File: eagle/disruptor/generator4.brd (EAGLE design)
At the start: 126.5 x 120.7 mm, 35 parts, among them IC1 NE555, IC2 74ALS04N, IC3 IR2110, IC4 7805TV, J1 PIN2F061.100, J2 PIN2F061.100, J3 PIN2F061.100, J4 PIN2F061.100, J5 PIN2F061.100, J6 PIN2F061.100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

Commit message: gen4b
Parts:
- added C14, C15: 1u, rcl:E5-8,5
- R6, R7: value 1M -> 22k
- moved J1 2.34 mm to (69.1, 19.1)
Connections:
- new net N$8: C14.-, C15.+, J2.A1, J2.A2
- net GND: now also C15.-; no longer J2.A1, J2.A2
- net N$6: now also C14.+
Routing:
- net TRANS: track 24.1 -> 207.0 mm
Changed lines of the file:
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@@
 <element name="R4" library="rcl" package="0207/10" value="100" x="45.72" y="29.21"/>
 <element name="R5" library="rcl" package="0207/10" value="100" x="50.8" y="10.16" rot="R90"/>
-<element name="J1" library="con-faston" package="F061.100" value="PIN2F061.100" x="68.58" y="21.336" rot="R180">
-<attribute name="OC_NEWARK" value="unknown" x="68.58" y="21.336" size="1.778" layer="27" rot="R180" display="off"/>
-<attribute name="MPN" value="" x="68.58" y="21.336" size="1.778" layer="27" rot="R180" display="off"/>
-<attribute name="MF" value="" x="68.58" y="21.336" size="1.778" layer="27" rot="R180" display="off"/>
-<attribute name="OC_FARNELL" value="unknown" x="68.58" y="21.336" size="1.778" layer="27" rot="R180" display="off"/>
+<element name="J1" library="con-faston" package="F061.100" value="PIN2F061.100" x="69.088" y="19.05" rot="R180">
+<attribute name="OC_NEWARK" value="unknown" x="69.088" y="19.05" size="1.778" layer="27" rot="R180" display="off"/>
+<attribute name="MPN" value="" x="69.088" y="19.05" size="1.778" layer="27" rot="R180" display="off"/>
+<attribute name="MF" value="" x="69.088" y="19.05" size="1.778" layer="27" rot="R180" display="off"/>
+<attribute name="OC_FARNELL" value="unknown" x="69.088" y="19.05" size="1.778" layer="27" rot="R180" display="off"/>
 </element>
 <element name="J2" library="con-faston" package="F061.100" value="PIN2F061.100" x="68.58" y="5.588" rot="R180">
@@
 <attribute name="OC_FARNELL" value="unknown" x="-40.386" y="86.868" size="1.778" layer="27" display="off"/>
 </element>
-<element name="R6" library="rcl" package="0207/10" value="1M" x="36.576" y="24.13" rot="R270"/>
-<element name="R7" library="rcl" package="0207/10" value="1M" x="18.288" y="5.08" rot="R180"/>
+<element name="R6" library="rcl" package="0207/10" value="22k" x="36.576" y="24.13" rot="R270"/>
+<element name="R7" library="rcl" package="0207/10" value="22k" x="18.288" y="5.08" rot="R180"/>
 <element name="C3" library="rcl" package="C075-052X106" value="10n" x="29.972" y="64.77" rot="R180"/>
 <element name="C6" library="rcl" package="C075-052X106" value="10n" x="53.848" y="42.926" rot="R180"/>
@@
 <element name="B2" library="rectifier" package="GBU4" value="RECTIFIER-GBU4" x="-22.86" y="78.994" rot="R270"/>
 <element name="C13" library="resistor" package="E7,5-18" value="" x="-2.286" y="106.934" rot="R90"/>
+<element name="C14" library="rcl" package="E5-8,5" value="1u" x="92.71" y="7.874" rot="R270"/>
+<element name="C15" library="rcl" package="E5-8,5" value="1u" x="94.996" y="23.622" rot="R90"/>
 </elements>
 <signals>
@@
 <contactref element="C2" pad="-"/>
 <contactref element="C4" pad="-"/>
-<contactref element="Q2" pad="S"/>
 <contactref element="R7" pad="2"/>
 <contactref element="C3" pad="1"/>
@@
 <wire x1="60.198" y1="58.674" x2="55.118" y2="53.594" width="1.6764" layer="16"/>
 <wire x1="55.118" y1="53.594" x2="55.118" y2="50.038" width="1.6764" layer="16"/>
-<contactref element="J2" pad="A1"/>
-<contactref element="J2" pad="A2"/>
+<contactref element="C15" pad="-"/>
+<contactref element="Q2" pad="S"/>
+<wire x1="60.198" y1="63.5" x2="60.198" y2="71.12" width="0" layer="19" extent="1-1"/>
+<wire x1="94.996" y1="26.162" x2="57.658" y2="42.926" width="0" layer="19" extent="1-1"/>
 </signal>
 <signal name="VCC">
@@
 <wire x1="22.098" y1="19.05" x2="36.576" y2="19.05" width="1.6764" layer="1"/>
 <wire x1="52.578" y1="80.01" x2="52.578" y2="77.47" width="2.54" layer="1"/>
-<wire x1="52.578" y1="77.47" x2="52.578" y2="70.358" width="1.6764" layer="1"/>
+<wire x1="36.576" y1="19.05" x2="31.75" y2="19.05" width="1.6764" layer="1"/>
+<wire x1="31.75" y1="19.05" x2="31.75" y2="7.62" width="1.6764" layer="1"/>
+<wire x1="31.75" y1="7.62" x2="37.084" y2="7.62" width="1.6764" layer="1"/>
+<wire x1="52.578" y1="70.358" x2="52.578" y2="77.47" width="1.6764" layer="1"/>
+<wire x1="71.12" y1="74.93" x2="71.12" y2="20.828" width="2.54" layer="1"/>
+<wire x1="36.576" y1="19.05" x2="56.134" y2="19.05" width="2.54" layer="1"/>
+<wire x1="56.134" y1="19.05" x2="66.588" y2="19.05" width="2.54" layer="1"/>
+<wire x1="71.12" y1="74.93" x2="53.086" y2="74.93" width="2.54" layer="1"/>
+<wire x1="66.588" y1="19.05" x2="74.168" y2="19.05" width="1.6764" layer="1"/>
+<wire x1="74.168" y1="19.05" x2="74.168" y2="21.082" width="1.6764" layer="1"/>
+<wire x1="74.168" y1="21.082" x2="63.754" y2="21.082" width="1.6764" layer="1"/>
+<wire x1="63.754" y1="21.082" x2="63.5" y2="20.828" width="1.6764" layer="1"/>
+<wire x1="63.5" y1="20.828" x2="63.5" y2="17.018" width="1.6764" layer="1"/>
+<wire x1="63.5" y1="17.018" x2="74.168" y2="17.018" width="1.6764" layer="1"/>
+<wire x1="74.168" y1="17.018" x2="74.168" y2="19.304" width="1.6764" layer="1"/>
+<wire x1="74.168" y1="19.304" x2="73.914" y2="19.558" width="1.6764" layer="1"/>
+<wire x1="73.914" y1="19.558" x2="64.77" y2="19.558" width="1.6764" layer="1"/>
+<wire x1="64.77" y1="19.558" x2="64.262" y2="20.066" width="1.6764" layer="1"/>
+<wire x1="64.262" y1="20.066" x2="64.262" y2="18.034" width="1.6764" layer="1"/>
+<wire x1="64.262" y1="18.034" x2="64.516" y2="17.78" width="1.6764" layer="1"/>
+<wire x1="64.516" y1="17.78" x2="73.914" y2="17.78" width="1.6764" layer="1"/>
 <wire x1="52.578" y1="70.358" x2="52.578" y2="71.12" width="0" layer="19" extent="1-1"/>
-<wire x1="66.08" y1="21.336" x2="52.578" y2="70.358" width="0" layer="19" extent="1-1"/>
-<wire x1="71.08" y1="21.336" x2="66.08" y2="21.336" width="0" layer="19" extent="1-1"/>
-<wire x1="36.576" y1="19.05" x2="66.08" y2="21.336" width="0" layer="19" extent="1-1"/>
-<wire x1="36.068" y1="7.62" x2="36.576" y2="19.05" width="0" layer="19" extent="1-1"/>
+<wire x1="53.086" y1="74.93" x2="52.578" y2="77.47" width="0" layer="19" extent="1-1"/>
+<wire x1="71.588" y1="19.05" x2="71.12" y2="20.828" width="0" layer="19" extent="1-1"/>
+<wire x1="73.914" y1="19.558" x2="71.588" y2="19.05" width="0" layer="19" extent="1-1"/>
+<wire x1="36.068" y1="7.62" x2="37.084" y2="7.62" width="0" layer="19" extent="1-1"/>
 </signal>
 <signal name="N$3">
@@
 <wire x1="10.414" y1="18.542" x2="13.462" y2="21.59" width="2.54" layer="1"/>
 <wire x1="13.462" y1="21.59" x2="22.606" y2="21.59" width="1.6764" layer="1"/>
-<wire x1="22.606" y1="21.59" x2="22.098" y2="21.59" width="0" layer="19" extent="1-1"/>
+<contactref element="C14" pad="+"/>
+<wire x1="22.606" y1="21.59" x2="92.71" y2="10.414" width="0" layer="19" extent="1-1"/>
+<wire x1="22.098" y1="21.59" x2="22.606" y2="21.59" width="0" layer="19" extent="1-1"/>
+</signal>
+<signal name="N$8">
+<contactref element="J2" pad="A1"/>
+<contactref element="J2" pad="A2"/>
+<contactref element="C15" pad="+"/>
+<contactref element="C14" pad="-"/>
+<wire x1="92.71" y1="5.334" x2="94.996" y2="21.082" width="0" layer="19" extent="1-1"/>
+<wire x1="71.08" y1="5.588" x2="92.71" y2="5.334" width="0" layer="19" extent="1-1"/>
+<wire x1="66.08" y1="5.588" x2="71.08" y2="5.588" width="0" layer="19" extent="1-1"/>
 </signal>
 </signals>

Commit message: generator 4 is the correct way.
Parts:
- C14, C15: value 1u -> 50u
- C7: value 1u -> min 12 nF
- R4, R5: value 100 -> 10
- moved C15 39.9 mm to (55.9, 16.0), turned to 180 degrees
- moved C14 36.9 mm to (55.9, 5.84), turned to 0 degrees
- moved J1 5.59 mm to (68.8, 24.6)
- moved R5 4.58 mm to (46.2, 9.91)
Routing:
- net TRANS: track 207.0 -> 27.7 mm
- net LO: track 69.6 -> 1.52 mm
- net N$11: track 29.5 -> 2.03 mm
- net N$12: track 20.6 -> 0.00 mm
- net HO: track 72.2 -> 54.9 mm
- net N$6: track 91.1 -> 77.6 mm
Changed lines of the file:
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@@
 <element name="D1" library="diode" package="D-7.5" value="UF4004" x="57.658" y="88.9"/>
 <element name="C8" library="rcl" package="E5-8,5" value="1u" x="61.468" y="82.296" rot="R270"/>
-<element name="C7" library="rcl" package="E5-8,5" value="1u" x="50.038" y="80.01"/>
+<element name="C7" library="rcl" package="E5-8,5" value="min 12 nF" x="50.038" y="80.01"/>
 <element name="IC1" library="st-microelectronics" package="DIL-08" value="NE555" x="17.018" y="59.69">
 <attribute name="OC_NEWARK" value="89K1486" x="76.708" y="-11.43" size="1.778" layer="27" display="off"/>
@@
 <element name="C4" library="rcl" package="E5-8,5" value="1u" x="67.818" y="112.014" rot="R270"/>
 <element name="C5" library="rcl" package="E5-8,5" value="1u" x="67.818" y="99.06" rot="R90"/>
-<element name="R4" library="rcl" package="0207/10" value="100" x="45.72" y="29.21"/>
-<element name="R5" library="rcl" package="0207/10" value="100" x="50.8" y="10.16" rot="R90"/>
-<element name="J1" library="con-faston" package="F061.100" value="PIN2F061.100" x="69.088" y="19.05" rot="R180">
-<attribute name="OC_NEWARK" value="unknown" x="69.088" y="19.05" size="1.778" layer="27" rot="R180" display="off"/>
-<attribute name="MPN" value="" x="69.088" y="19.05" size="1.778" layer="27" rot="R180" display="off"/>
-<attribute name="MF" value="" x="69.088" y="19.05" size="1.778" layer="27" rot="R180" display="off"/>
-<attribute name="OC_FARNELL" value="unknown" x="69.088" y="19.05" size="1.778" layer="27" rot="R180" display="off"/>
+<element name="R4" library="rcl" package="0207/10" value="10" x="45.72" y="29.21"/>
+<element name="R5" library="rcl" package="0207/10" value="10" x="46.228" y="9.906" rot="R90"/>
+<element name="J1" library="con-faston" package="F061.100" value="PIN2F061.100" x="68.834" y="24.638" rot="R180">
+<attribute name="OC_NEWARK" value="unknown" x="68.834" y="24.638" size="1.778" layer="27" rot="R180" display="off"/>
+<attribute name="MPN" value="" x="68.834" y="24.638" size="1.778" layer="27" rot="R180" display="off"/>
+<attribute name="MF" value="" x="68.834" y="24.638" size="1.778" layer="27" rot="R180" display="off"/>
+<attribute name="OC_FARNELL" value="unknown" x="68.834" y="24.638" size="1.778" layer="27" rot="R180" display="off"/>
 </element>
 <element name="J2" library="con-faston" package="F061.100" value="PIN2F061.100" x="68.58" y="5.588" rot="R180">
@@
 <element name="B2" library="rectifier" package="GBU4" value="RECTIFIER-GBU4" x="-22.86" y="78.994" rot="R270"/>
 <element name="C13" library="resistor" package="E7,5-18" value="" x="-2.286" y="106.934" rot="R90"/>
-<element name="C14" library="rcl" package="E5-8,5" value="1u" x="92.71" y="7.874" rot="R270"/>
-<element name="C15" library="rcl" package="E5-8,5" value="1u" x="94.996" y="23.622" rot="R90"/>
+<element name="C14" library="rcl" package="E5-8,5" value="50u" x="55.88" y="5.842"/>
+<element name="C15" library="rcl" package="E5-8,5" value="50u" x="55.88" y="16.002" rot="R180"/>
 </elements>
 <signals>
@@
 <contactref element="Q2" pad="S"/>
 <wire x1="60.198" y1="63.5" x2="60.198" y2="71.12" width="0" layer="19" extent="1-1"/>
-<wire x1="94.996" y1="26.162" x2="57.658" y2="42.926" width="0" layer="19" extent="1-1"/>
 </signal>
 <signal name="VCC">
@@
 <contactref element="IC3" pad="1"/>
 <contactref element="R5" pad="2"/>
-<wire x1="62.738" y1="33.02" x2="50.8" y2="21.59" width="1.6764" layer="16"/>
-<wire x1="50.8" y1="21.59" x2="50.8" y2="15.24" width="1.6764" layer="16"/>
 <wire x1="62.738" y1="71.12" x2="62.738" y2="72.644" width="1.6764" layer="16"/>
-<wire x1="62.738" y1="71.12" x2="62.738" y2="67.31" width="1.6764" layer="16"/>
-<wire x1="62.738" y1="67.31" x2="66.294" y2="67.31" width="1.6764" layer="16"/>
-<wire x1="66.294" y1="67.31" x2="66.294" y2="33.02" width="1.6764" layer="16"/>
-<wire x1="66.294" y1="33.02" x2="62.738" y2="33.02" width="1.6764" layer="16"/>
+<wire x1="46.228" y1="14.986" x2="62.738" y2="71.12" width="0" layer="19" extent="1-1"/>
 </signal>
 <signal name="HO">
@@
 <wire x1="47.498" y1="67.31" x2="65.532" y2="67.31" width="1.6764" layer="1"/>
 <wire x1="65.532" y1="67.31" x2="65.532" y2="35.56" width="2.54" layer="1"/>
-<wire x1="65.532" y1="35.56" x2="57.15" y2="35.56" width="2.54" layer="1"/>
-<wire x1="57.15" y1="35.56" x2="50.8" y2="29.21" width="2.54" layer="1"/>
+<wire x1="50.8" y1="29.21" x2="65.532" y2="35.56" width="0" layer="19" extent="1-1"/>
 </signal>
 <signal name="N$17">
@@
 <contactref element="Q2" pad="G"/>
 <contactref element="R7" pad="1"/>
-<wire x1="23.368" y1="5.08" x2="36.068" y2="5.08" width="1.6764" layer="1"/>
 <wire x1="36.068" y1="5.08" x2="38.1" y2="5.08" width="1.6764" layer="1"/>
-<wire x1="36.068" y1="5.08" x2="50.8" y2="5.08" width="1.6764" layer="1"/>
+<wire x1="38.1" y1="5.08" x2="46.228" y2="4.826" width="0" layer="19" extent="1-1"/>
+<wire x1="23.368" y1="5.08" x2="36.068" y2="5.08" width="0" layer="19" extent="1-1"/>
 </signal>
 <signal name="N$12">
@@
 <contactref element="R4" pad="1"/>
 <contactref element="R6" pad="1"/>
-<wire x1="22.098" y1="24.13" x2="31.496" y2="24.13" width="1.6764" layer="1"/>
-<wire x1="31.496" y1="24.13" x2="36.576" y2="29.21" width="1.6764" layer="1"/>
-<wire x1="36.576" y1="29.21" x2="40.64" y2="29.21" width="1.6764" layer="1"/>
+<wire x1="36.576" y1="29.21" x2="40.64" y2="29.21" width="0" layer="19" extent="1-1"/>
+<wire x1="22.098" y1="24.13" x2="36.576" y2="29.21" width="0" layer="19" extent="1-1"/>
 </signal>
 <signal name="TRANS">
@@
 <contactref element="J1" pad="A1"/>
 <contactref element="J1" pad="A2"/>
-<wire x1="22.098" y1="19.05" x2="36.576" y2="19.05" width="1.6764" layer="1"/>
 <wire x1="52.578" y1="80.01" x2="52.578" y2="77.47" width="2.54" layer="1"/>
-<wire x1="36.576" y1="19.05" x2="31.75" y2="19.05" width="1.6764" layer="1"/>
-<wire x1="31.75" y1="19.05" x2="31.75" y2="7.62" width="1.6764" layer="1"/>
-<wire x1="31.75" y1="7.62" x2="37.084" y2="7.62" width="1.6764" layer="1"/>
 <wire x1="52.578" y1="70.358" x2="52.578" y2="77.47" width="1.6764" layer="1"/>
-<wire x1="71.12" y1="74.93" x2="71.12" y2="20.828" width="2.54" layer="1"/>
-<wire x1="36.576" y1="19.05" x2="56.134" y2="19.05" width="2.54" layer="1"/>
-<wire x1="56.134" y1="19.05" x2="66.588" y2="19.05" width="2.54" layer="1"/>
 <wire x1="71.12" y1="74.93" x2="53.086" y2="74.93" width="2.54" layer="1"/>
-<wire x1="66.588" y1="19.05" x2="74.168" y2="19.05" width="1.6764" layer="1"/>
-<wire x1="74.168" y1="19.05" x2="74.168" y2="21.082" width="1.6764" layer="1"/>
-<wire x1="74.168" y1="21.082" x2="63.754" y2="21.082" width="1.6764" layer="1"/>
-<wire x1="63.754" y1="21.082" x2="63.5" y2="20.828" width="1.6764" layer="1"/>
-<wire x1="63.5" y1="20.828" x2="63.5" y2="17.018" width="1.6764" layer="1"/>
-<wire x1="63.5" y1="17.018" x2="74.168" y2="17.018" width="1.6764" layer="1"/>
-<wire x1="74.168" y1="17.018" x2="74.168" y2="19.304" width="1.6764" layer="1"/>
-<wire x1="74.168" y1="19.304" x2="73.914" y2="19.558" width="1.6764" layer="1"/>
-<wire x1="73.914" y1="19.558" x2="64.77" y2="19.558" width="1.6764" layer="1"/>
-<wire x1="64.77" y1="19.558" x2="64.262" y2="20.066" width="1.6764" layer="1"/>
-<wire x1="64.262" y1="20.066" x2="64.262" y2="18.034" width="1.6764" layer="1"/>
-<wire x1="64.262" y1="18.034" x2="64.516" y2="17.78" width="1.6764" layer="1"/>
-<wire x1="64.516" y1="17.78" x2="73.914" y2="17.78" width="1.6764" layer="1"/>
-<wire x1="52.578" y1="70.358" x2="52.578" y2="71.12" width="0" layer="19" extent="1-1"/>
-<wire x1="53.086" y1="74.93" x2="52.578" y2="77.47" width="0" layer="19" extent="1-1"/>
-<wire x1="71.588" y1="19.05" x2="71.12" y2="20.828" width="0" layer="19" extent="1-1"/>
-<wire x1="73.914" y1="19.558" x2="71.588" y2="19.05" width="0" layer="19" extent="1-1"/>
-<wire x1="36.068" y1="7.62" x2="37.084" y2="7.62" width="0" layer="19" extent="1-1"/>
+<wire x1="52.578" y1="77.47" x2="53.086" y2="74.93" width="0" layer="19" extent="1-1"/>
+<wire x1="52.578" y1="71.12" x2="52.578" y2="70.358" width="0" layer="19" extent="1-1"/>
+<wire x1="66.334" y1="24.638" x2="52.578" y2="70.358" width="0" layer="19" extent="1-1"/>
+<wire x1="71.334" y1="24.638" x2="66.334" y2="24.638" width="0" layer="19" extent="1-1"/>
+<wire x1="36.576" y1="19.05" x2="66.334" y2="24.638" width="0" layer="19" extent="1-1"/>
+<wire x1="36.068" y1="7.62" x2="36.576" y2="19.05" width="0" layer="19" extent="1-1"/>
+<wire x1="22.098" y1="19.05" x2="36.576" y2="19.05" width="0" layer="19" extent="1-1"/>
 </signal>
 <signal name="N$3">
@@
 <wire x1="-25.908" y1="40.386" x2="-4.064" y2="18.542" width="2.54" layer="1"/>
 <wire x1="-4.064" y1="18.542" x2="10.414" y2="18.542" width="2.54" layer="1"/>
-<wire x1="10.414" y1="18.542" x2="13.462" y2="21.59" width="2.54" layer="1"/>
-<wire x1="13.462" y1="21.59" x2="22.606" y2="21.59" width="1.6764" layer="1"/>
 <contactref element="C14" pad="+"/>
-<wire x1="22.606" y1="21.59" x2="92.71" y2="10.414" width="0" layer="19" extent="1-1"/>
-<wire x1="22.098" y1="21.59" x2="22.606" y2="21.59" width="0" layer="19" extent="1-1"/>
+<wire x1="22.098" y1="21.59" x2="53.34" y2="5.842" width="0" layer="19" extent="1-1"/>
+<wire x1="10.414" y1="18.542" x2="22.098" y2="21.59" width="0" layer="19" extent="1-1"/>
 </signal>
 <signal name="N$8">
@@
 <contactref element="C15" pad="+"/>
 <contactref element="C14" pad="-"/>
-<wire x1="92.71" y1="5.334" x2="94.996" y2="21.082" width="0" layer="19" extent="1-1"/>
-<wire x1="71.08" y1="5.588" x2="92.71" y2="5.334" width="0" layer="19" extent="1-1"/>
 <wire x1="66.08" y1="5.588" x2="71.08" y2="5.588" width="0" layer="19" extent="1-1"/>
+<wire x1="58.42" y1="5.842" x2="66.08" y2="5.588" width="0" layer="19" extent="1-1"/>
+<wire x1="58.42" y1="16.002" x2="58.42" y2="5.842" width="0" layer="19" extent="1-1"/>
 </signal>
 </signals>

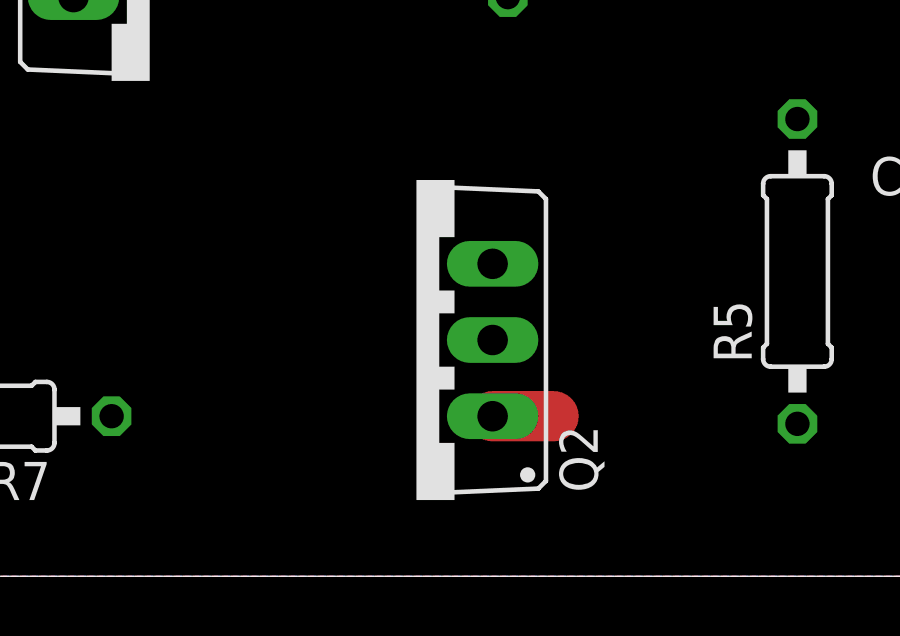
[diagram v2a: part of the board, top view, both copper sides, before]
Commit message: use generator 4
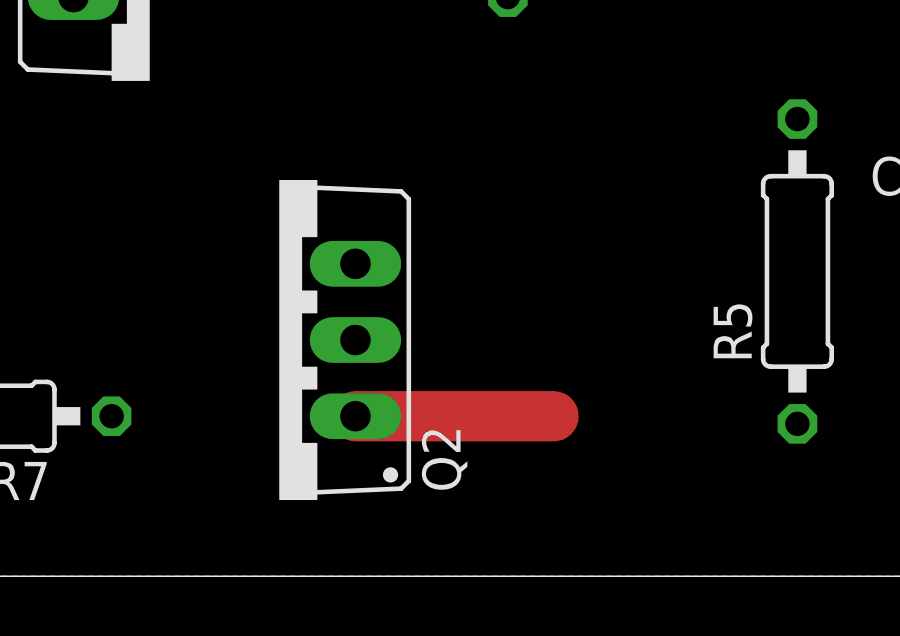
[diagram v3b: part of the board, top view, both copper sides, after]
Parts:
- moved Q2 4.57 mm to (29.0, 7.62)
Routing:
- net N$11: track 2.03 -> 6.60 mm
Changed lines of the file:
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@@
 <element name="C2" library="rcl" package="E5-8,5" value=".1u" x="1.778" y="56.896" rot="R180"/>
 <element name="Q1" library="transistor-power" package="TO220BV" value="STP11NM60" x="24.638" y="21.59" rot="R270"/>
-<element name="Q2" library="transistor-power" package="TO220BV" value="STP11NM60" x="33.528" y="7.62" rot="R90"/>
+<element name="Q2" library="transistor-power" package="TO220BV" value="STP11NM60" x="28.956" y="7.62" rot="R90"/>
 <element name="C4" library="rcl" package="E5-8,5" value="1u" x="67.818" y="112.014" rot="R270"/>
 <element name="C5" library="rcl" package="E5-8,5" value="1u" x="67.818" y="99.06" rot="R90"/>
@@
 <contactref element="Q2" pad="G"/>
 <contactref element="R7" pad="1"/>
-<wire x1="36.068" y1="5.08" x2="38.1" y2="5.08" width="1.6764" layer="1"/>
+<wire x1="31.496" y1="5.08" x2="38.1" y2="5.08" width="1.6764" layer="1"/>
 <wire x1="38.1" y1="5.08" x2="46.228" y2="4.826" width="0" layer="19" extent="1-1"/>
-<wire x1="23.368" y1="5.08" x2="36.068" y2="5.08" width="0" layer="19" extent="1-1"/>
+<wire x1="23.368" y1="5.08" x2="31.496" y2="5.08" width="0" layer="19" extent="1-1"/>
 </signal>
 <signal name="N$12">
@@
 <wire x1="71.334" y1="24.638" x2="66.334" y2="24.638" width="0" layer="19" extent="1-1"/>
 <wire x1="36.576" y1="19.05" x2="66.334" y2="24.638" width="0" layer="19" extent="1-1"/>
-<wire x1="36.068" y1="7.62" x2="36.576" y2="19.05" width="0" layer="19" extent="1-1"/>
+<wire x1="31.496" y1="7.62" x2="36.576" y2="19.05" width="0" layer="19" extent="1-1"/>
 <wire x1="22.098" y1="19.05" x2="36.576" y2="19.05" width="0" layer="19" extent="1-1"/>
 </signal>
